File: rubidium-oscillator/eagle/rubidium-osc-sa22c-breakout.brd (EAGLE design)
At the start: 49.8 x 56.6 mm, 13 parts, among them J1 OSC_TMMH-109-01-G-DV-ES-A, Q1 FDN360P, Q2 FDN360P, X1 MKDSN4, X2 MPT3, X3 MPT6, X4 SMA-142-0701-801/806, X5 SMA-142-0701-801/806, X6 SMA-142-0701-801/806

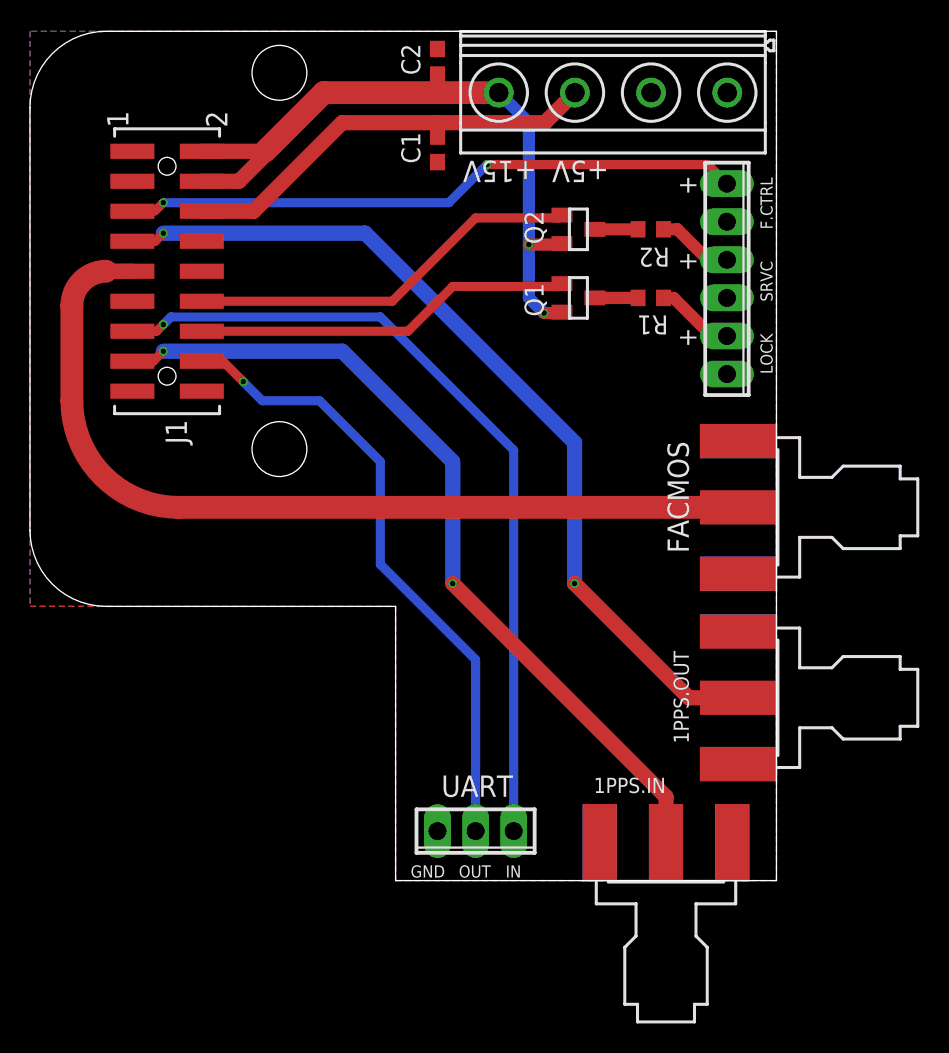
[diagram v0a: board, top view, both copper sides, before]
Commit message: Updated rubidium osc.  Removed thermal reliefs for SMA and power grounds.  Updated p-MOSFET design.
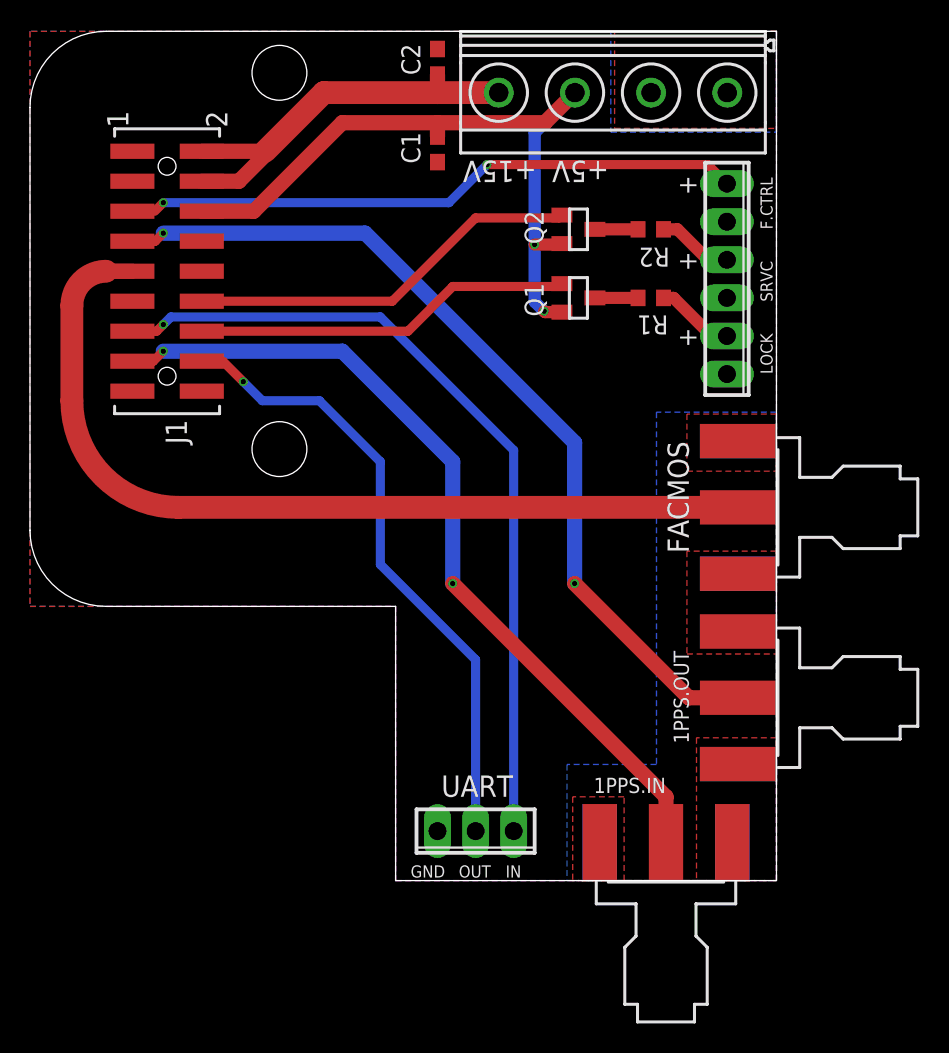
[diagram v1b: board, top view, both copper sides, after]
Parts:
- Q1, Q2: value FDN360P -> ZXMP10A13F
- R1: value 4.7k -> 560
- R2: value 5.6k -> 1k
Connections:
- net +15V: no longer Q1.2, Q2.2
- net +5V: now also Q1.2, Q2.2
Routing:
- net +15V: track 47.8 -> 28.4 mm, vias 2 -> 0
- net +5V: track 29.1 -> 48.1 mm, vias 0 -> 2
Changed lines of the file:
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@@
 <attribute name="NAME" x="9.044" y="12.452" size="1.4224" layer="21" font="vector" ratio="15" rot="R270"/>
 </element>
-<element name="Q1" library="transistor-power" library_urn="urn:adsk.eagle:library:400" package="SUPER-SOT3" package3d_urn="urn:adsk.eagle:package:29529/2" value="FDN360P" x="36.576" y="20.574" smashed="yes" rot="R270">
+<element name="Q1" library="transistor-power" library_urn="urn:adsk.eagle:library:400" package="SUPER-SOT3" package3d_urn="urn:adsk.eagle:package:29529/2" value="ZXMP10A13F" x="36.576" y="20.574" smashed="yes" rot="R270">
 <attribute name="NAME" x="32.988" y="21.562" size="1.27" layer="25" rot="R270"/>
 </element>
-<element name="Q2" library="transistor-power" library_urn="urn:adsk.eagle:library:400" package="SUPER-SOT3" package3d_urn="urn:adsk.eagle:package:29529/2" value="FDN360P" x="36.576" y="25.146" smashed="yes" rot="R270">
+<element name="Q2" library="transistor-power" library_urn="urn:adsk.eagle:library:400" package="SUPER-SOT3" package3d_urn="urn:adsk.eagle:package:29529/2" value="ZXMP10A13F" x="36.576" y="25.146" smashed="yes" rot="R270">
 <attribute name="NAME" x="32.988" y="26.388" size="1.27" layer="25" rot="R270"/>
 </element>
-<element name="R1" library="rcl" library_urn="urn:adsk.eagle:library:334" package="R0603" package3d_urn="urn:adsk.eagle:package:23555/3" value="4.7k" x="41.402" y="20.574" smashed="yes" rot="R180">
+<element name="R1" library="rcl" library_urn="urn:adsk.eagle:library:334" package="R0603" package3d_urn="urn:adsk.eagle:package:23555/3" value="560" x="41.402" y="20.574" smashed="yes" rot="R180">
 <attribute name="NAME" x="42.5704" y="19.4056" size="1.27" layer="25" rot="SR180"/>
 <attribute name="SPICEPREFIX" value="R" x="-19.558" y="92.964" size="1.778" layer="27" rot="R180" display="off"/>
 </element>
-<element name="R2" library="rcl" library_urn="urn:adsk.eagle:library:334" package="R0603" package3d_urn="urn:adsk.eagle:package:23555/3" value="5.6k" x="41.402" y="25.146" smashed="yes" rot="R180">
+<element name="R2" library="rcl" library_urn="urn:adsk.eagle:library:334" package="R0603" package3d_urn="urn:adsk.eagle:package:23555/3" value="1k" x="41.402" y="25.146" smashed="yes" rot="R180">
 <attribute name="NAME" x="42.672" y="23.9268" size="1.27" layer="25" rot="SR180"/>
 <attribute name="SPICEPREFIX" value="R" x="24.892" y="105.156" size="1.778" layer="27" rot="R180" display="off"/>
@@
 <vertex x="49.784" y="38.354"/>
 </polygon>
+<polygon width="0.1524" layer="1" thermals="no">
+<vertex x="43.815" y="12.827"/>
+<vertex x="43.815" y="9.017"/>
+<vertex x="49.784" y="9.017"/>
+<vertex x="49.784" y="12.827"/>
+</polygon>
+<polygon width="0.1524" layer="1" thermals="no">
+<vertex x="43.815" y="3.683"/>
+<vertex x="43.815" y="-3.175"/>
+<vertex x="49.784" y="-3.175"/>
+<vertex x="49.784" y="3.683"/>
+</polygon>
+<polygon width="0.1524" layer="1" thermals="no">
+<vertex x="44.45" y="-8.763"/>
+<vertex x="44.45" y="-18.288"/>
+<vertex x="49.784" y="-18.288"/>
+<vertex x="49.784" y="-8.763"/>
+</polygon>
+<polygon width="0.1524" layer="1" thermals="no">
+<vertex x="36.195" y="-12.7"/>
+<vertex x="36.195" y="-18.288"/>
+<vertex x="39.624" y="-18.288"/>
+<vertex x="39.624" y="-12.7"/>
+</polygon>
+<polygon width="0.1524" layer="1" thermals="no">
+<vertex x="38.989" y="38.354"/>
+<vertex x="38.989" y="31.877"/>
+<vertex x="49.784" y="31.877"/>
+<vertex x="49.784" y="38.354"/>
+</polygon>
+<polygon width="0.1524" layer="16" thermals="no">
+<vertex x="38.735" y="38.354"/>
+<vertex x="38.735" y="31.623"/>
+<vertex x="49.784" y="31.623"/>
+<vertex x="49.784" y="38.354"/>
+</polygon>
+<polygon width="0.1524" layer="16" thermals="no">
+<vertex x="35.814" y="-18.288"/>
+<vertex x="49.784" y="-18.288"/>
+<vertex x="49.784" y="12.954"/>
+<vertex x="41.783" y="12.954"/>
+<vertex x="41.783" y="-10.541"/>
+<vertex x="35.814" y="-10.541"/>
+</polygon>
 </signal>
 <signal name="+15V">
 <contactref element="J1" pad="2"/>
 <contactref element="J1" pad="4"/>
-<contactref element="Q1" pad="2"/>
-<contactref element="Q2" pad="2"/>
 <contactref element="C2" pad="1"/>
 <contactref element="X1" pad="4"/>
@@
 <wire x1="27.178" y1="34.265" x2="19.59375625" y2="34.265" width="1.524" layer="1"/>
 <wire x1="27.178" y1="35.472" x2="27.178" y2="34.265" width="1.016" layer="1"/>
-<wire x1="31.2631" y1="34.265" x2="33.274" y2="32.2541" width="0.8128" layer="16"/>
-<wire x1="35.41" y1="19.558" x2="35.476" y2="19.624" width="0.8128" layer="1"/>
-<wire x1="33.274" y1="32.2541" x2="33.274" y2="24.13" width="0.8128" layer="16"/>
-<wire x1="33.274" y1="24.13" x2="33.274" y2="20.574" width="0.8128" layer="16"/>
-<wire x1="33.274" y1="20.574" x2="34.29" y2="19.558" width="0.8128" layer="16"/>
-<via x="34.29" y="19.558" extent="1-16" drill="0.35"/>
-<wire x1="34.29" y1="19.558" x2="35.41" y2="19.558" width="0.8128" layer="1"/>
-<via x="33.274" y="24.13" extent="1-16" drill="0.35"/>
-<wire x1="35.41" y1="24.13" x2="33.274" y2="24.13" width="0.8128" layer="1"/>
-<wire x1="35.476" y1="24.196" x2="35.41" y2="24.13" width="0.8128" layer="1"/>
 <wire x1="19.59375625" y1="34.265" x2="15.68075625" y2="30.352" width="1.524" layer="1"/>
 <wire x1="15.68075625" y1="30.352" x2="15.42675625" y2="30.352" width="1.016" layer="1"/>
@@
 <wire x1="20.828" y1="32.258" x2="14.922" y2="26.352" width="1.016" layer="1"/>
 <wire x1="14.922" y1="26.352" x2="11.459" y2="26.352" width="1.016" layer="1"/>
+<contactref element="Q1" pad="2"/>
+<contactref element="Q2" pad="2"/>
+<wire x1="36.3431" y1="34.265" x2="33.655" y2="31.5769" width="0.8128" layer="16"/>
+<wire x1="33.655" y1="20.32" x2="34.29" y2="19.685" width="0.8128" layer="16"/>
+<via x="34.29" y="19.685" extent="1-16" drill="0.35"/>
+<wire x1="34.29" y1="19.685" x2="34.351" y2="19.624" width="0.8128" layer="1"/>
+<wire x1="34.351" y1="19.624" x2="35.476" y2="19.624" width="0.8128" layer="1"/>
+<wire x1="33.655" y1="31.5769" x2="33.655" y2="24.13" width="0.8128" layer="16"/>
+<wire x1="33.655" y1="24.13" x2="33.655" y2="20.32" width="0.8128" layer="16"/>
+<via x="33.655" y="24.13" extent="1-16" drill="0.35"/>
+<wire x1="33.655" y1="24.13" x2="35.41" y2="24.13" width="0.8128" layer="1"/>
+<wire x1="35.41" y1="24.13" x2="35.476" y2="24.196" width="0.8128" layer="1"/>
 </signal>
 <signal name="N$1" class="1">
@@
 <mfgpreviewcolor name="substratecolor" color="0xFF786E46"/>
 </mfgpreviewcolors>
+<errors>
+</errors>
 </board>
 </drawing>
